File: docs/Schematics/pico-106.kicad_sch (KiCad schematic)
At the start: 22 parts, among them J1 MIDI in, J2 Debug, J3 Stereo line out, J4 Debug, Q1 2N2222A, SW1 RST, U1 Pico 2 (RP2350), U2 TL072, U3 H11L1

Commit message: Rename project pico-106
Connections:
- net MIDI 31250 baud 8-N-1: now also U1.27 (GPIO21); no longer U1.26 (GPIO20)
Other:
- company: https://github.com/AnotherJohnH/pico106 -> https://github.com/AnotherJohnH/pico-106
- title: pico106 -> pico-106
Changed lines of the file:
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@@
   (paper "A4")
   (title_block
-    (title "pico106")
-    (date "2024-10-26")
+    (title "pico-106")
+    (date "2024-10-27")
     (rev "0.01")
-    (company "https://github.com/AnotherJohnH/pico106")
+    (company "https://github.com/AnotherJohnH/pico-106")
   )
   (junction (at 220.98 62.23) (diameter 0) (color 0 0 0 0)
@@
     (stroke (width 0) (type default))
   )
-  (wire (pts (xy 46.99 63.5) (xy 40.64 63.5))
+  (wire (pts (xy 46.99 60.96) (xy 40.64 60.96))
     (stroke (width 0) (type default))
   )
@@
     (stroke (width 0) (type default))
   )
-  (wire (pts (xy 40.64 63.5) (xy 40.64 91.44))
-    (stroke (width 0) (type default))
-  )
+  (wire (pts (xy 40.64 60.96) (xy 40.64 91.44))
+    (stroke (width 0) (type default))
+  )

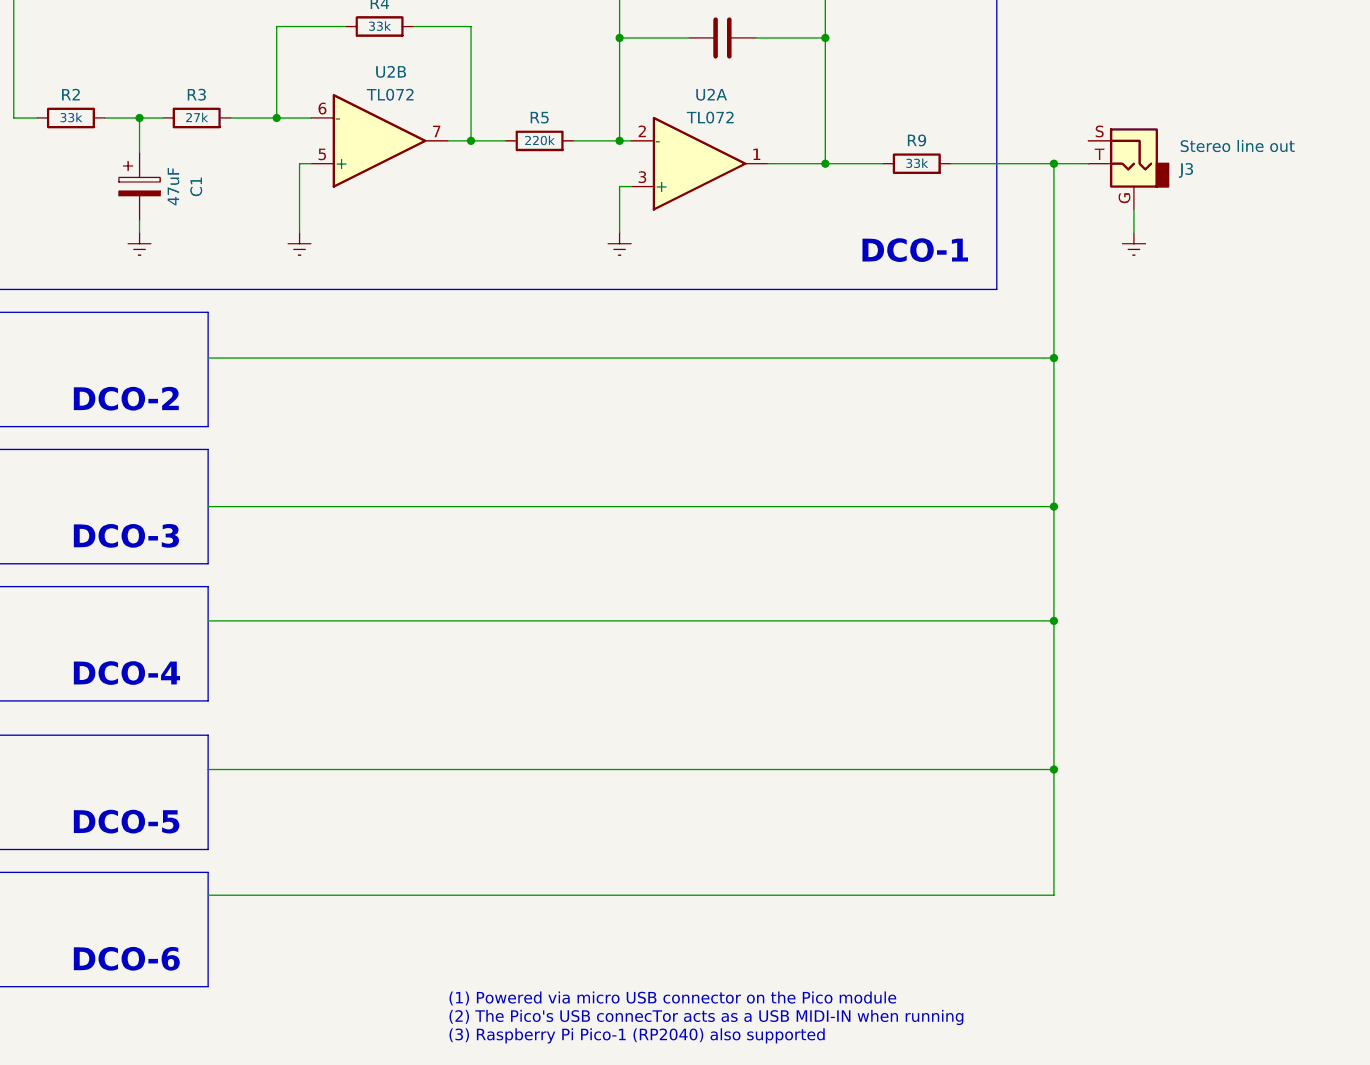
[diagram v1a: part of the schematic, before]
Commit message: Add initial spice model
  + also fixed wrong value for C1 on  schematic
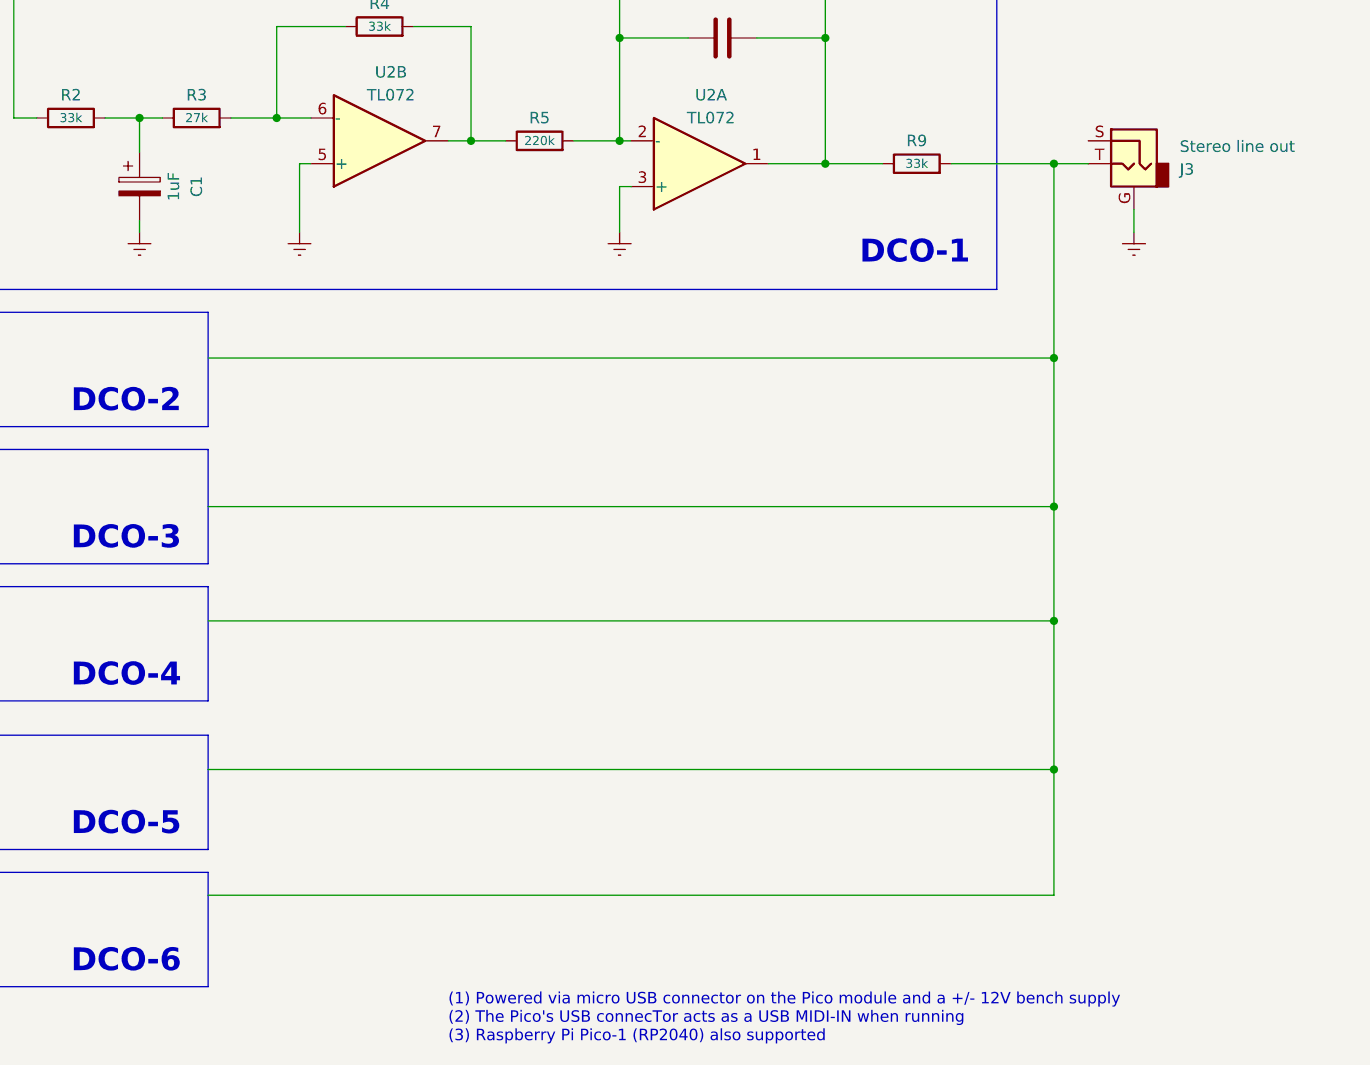
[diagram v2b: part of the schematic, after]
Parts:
- C1: value 47uF -> 1uF
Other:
- note added: "(1) Powered via micro USB connector on the Pico module and a +/- 12V bench supply (2) The Pico's USB connecTor acts as a USB MIDI-IN when running (3) Raspberry Pi Pico-1 (RP2040) also supported"
- note removed: "(1) Powered via micro USB connector on the Pico module (2) The Pico's USB connecTor acts as a USB MIDI-IN when running (3) Raspberry Pi Pico-1 (RP2040) also supported"
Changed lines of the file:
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@@
     (effects (font (size 2.54 2.54) (thickness 0.508) bold (color 84 84 84 1)) (justify left bottom))
   )
-  (text "(1) Powered via micro USB connector on the Pico module\n(2) The Pico's USB connecTor acts as a USB MIDI-IN when running\n(3) Raspberry Pi Pico-1 (RP2040) also supported"
+  (text "(1) Powered via micro USB connector on the Pico module and a +/- 12V bench supply\n(2) The Pico's USB connecTor acts as a USB MIDI-IN when running\n(3) Raspberry Pi Pico-1 (RP2040) also supported"
     (at 179.07 173.99 0)
     (effects (font (size 1.27 1.27)) (justify left bottom))
@@
     (pin "2")
     (instances
-      (project "pico106"
+      (project "pico-106"
         (path "/8dd66cb3-bd85-43a0-9ef0-1bd8a27e677c"
           (reference "R7") (unit 1)
@@
     (pin "2")
     (instances
-      (project "pico106"
+      (project "pico-106"
         (path "/8dd66cb3-bd85-43a0-9ef0-1bd8a27e677c"
           (reference "C3") (unit 1)
@@
     (pin "2")
     (instances
-      (project "pico106"
+      (project "pico-106"
         (path "/8dd66cb3-bd85-43a0-9ef0-1bd8a27e677c"
           (reference "D1") (unit 1)
@@
     (pin "9")
     (instances
-      (project "pico106"
+      (project "pico-106"
         (path "/8dd66cb3-bd85-43a0-9ef0-1bd8a27e677c"
           (reference "U1") (unit 1)
@@
     (pin "8")
     (instances
-      (project "pico106"
+      (project "pico-106"
         (path "/8dd66cb3-bd85-43a0-9ef0-1bd8a27e677c"
           (reference "U2") (unit 1)
@@
     (pin "1")
     (instances
-      (project "pico106"
+      (project "pico-106"
         (path "/8dd66cb3-bd85-43a0-9ef0-1bd8a27e677c"
           (reference "#PWR02") (unit 1)
@@
     (pin "2")
     (instances
-      (project "pico106"
+      (project "pico-106"
         (path "/8dd66cb3-bd85-43a0-9ef0-1bd8a27e677c"
           (reference "R5") (unit 1)
@@
     (pin "2")
     (instances
-      (project "pico106"
+      (project "pico-106"
         (path "/8dd66cb3-bd85-43a0-9ef0-1bd8a27e677c"
           (reference "R8") (unit 1)
@@
     (pin "3")
     (instances
-      (project "pico106"
+      (project "pico-106"
         (path "/8dd66cb3-bd85-43a0-9ef0-1bd8a27e677c"
           (reference "J2") (unit 1)
@@
     (pin "3")
     (instances
-      (project "pico106"
+      (project "pico-106"
         (path "/8dd66cb3-bd85-43a0-9ef0-1bd8a27e677c"
           (reference "Q1") (unit 1)
@@
     (pin "6")
     (instances
-      (project "pico106"
+      (project "pico-106"
         (path "/8dd66cb3-bd85-43a0-9ef0-1bd8a27e677c"
           (reference "U3") (unit 1)
@@
     (pin "1")
     (instances
-      (project "pico106"
+      (project "pico-106"
         (path "/8dd66cb3-bd85-43a0-9ef0-1bd8a27e677c"
           (reference "#PWR05") (unit 1)
@@
     (pin "2")
     (instances
-      (project "pico106"
+      (project "pico-106"
         (path "/8dd66cb3-bd85-43a0-9ef0-1bd8a27e677c"
           (reference "R2") (unit 1)
@@
     (pin "2")
     (instances
-      (project "pico106"
+      (project "pico-106"
         (path "/8dd66cb3-bd85-43a0-9ef0-1bd8a27e677c"
           (reference "SW1") (unit 1)
@@
     (pin "T")
     (instances
-      (project "pico106"
+      (project "pico-106"
         (path "/8dd66cb3-bd85-43a0-9ef0-1bd8a27e677c"
           (reference "J3") (unit 1)
@@
     (pin "1")
     (instances
-      (project "pico106"
+      (project "pico-106"
         (path "/8dd66cb3-bd85-43a0-9ef0-1bd8a27e677c"
           (reference "#PWR09") (unit 1)
@@
     (pin "1")
     (instances
-      (project "pico106"
+      (project "pico-106"
         (path "/8dd66cb3-bd85-43a0-9ef0-1bd8a27e677c"
           (reference "#PWR06") (unit 1)
@@
     (pin "2")
     (instances
-      (project "pico106"
+      (project "pico-106"
         (path "/8dd66cb3-bd85-43a0-9ef0-1bd8a27e677c"
           (reference "R3") (unit 1)
@@
     (pin "8")
     (instances
-      (project "pico106"
+      (project "pico-106"
         (path "/8dd66cb3-bd85-43a0-9ef0-1bd8a27e677c"
           (reference "U2") (unit 2)
@@
     (pin "1")
     (instances
-      (project "pico106"
+      (project "pico-106"
         (path "/8dd66cb3-bd85-43a0-9ef0-1bd8a27e677c"
           (reference "#PWR011") (unit 1)
@@
     (pin "2")
     (instances
-      (project "pico106"
+      (project "pico-106"
         (path "/8dd66cb3-bd85-43a0-9ef0-1bd8a27e677c"
           (reference "R9") (unit 1)
@@
     (pin "5")
     (instances
-      (project "pico106"
+      (project "pico-106"
         (path "/8dd66cb3-bd85-43a0-9ef0-1bd8a27e677c"
           (reference "J1") (unit 1)
@@
     (pin "2")
     (instances
-      (project "pico106"
+      (project "pico-106"
         (path "/8dd66cb3-bd85-43a0-9ef0-1bd8a27e677c"
           (reference "R1") (unit 1)
@@
     (pin "2")
     (instances
-      (project "pico106"
+      (project "pico-106"
         (path "/8dd66cb3-bd85-43a0-9ef0-1bd8a27e677c"
           (reference "C2") (unit 1)
@@
     (pin "2")
     (instances
-      (project "pico106"
+      (project "pico-106"
         (path "/8dd66cb3-bd85-43a0-9ef0-1bd8a27e677c"
           (reference "R4") (unit 1)
@@
       (effects (font (size 1.27 1.27)))
     )
-    (property "Value" "47uF" (at 148.59 78.74 90)
+    (property "Value" "1uF" (at 148.59 78.74 90)
       (effects (font (size 1.27 1.27)))
     )
@@
     (pin "2")
     (instances
-      (project "pico106"
+      (project "pico-106"
         (path "/8dd66cb3-bd85-43a0-9ef0-1bd8a27e677c"
           (reference "C1") (unit 1)
@@
     (pin "1")
     (instances
-      (project "pico106"
+      (project "pico-106"
         (path "/8dd66cb3-bd85-43a0-9ef0-1bd8a27e677c"
           (reference "#PWR08") (unit 1)
@@
     (pin "1")
     (instances
-      (project "pico106"
+      (project "pico-106"
         (path "/8dd66cb3-bd85-43a0-9ef0-1bd8a27e677c"
           (reference "#PWR01") (unit 1)
@@
     (pin "3")
     (instances
-      (project "pico106"
+      (project "pico-106"
         (path "/8dd66cb3-bd85-43a0-9ef0-1bd8a27e677c"
           (reference "J4") (unit 1)
@@
     (pin "1")
     (instances
-      (project "pico106"
+      (project "pico-106"
         (path "/8dd66cb3-bd85-43a0-9ef0-1bd8a27e677c"
           (reference "#PWR010") (unit 1)
@@
     (pin "1")
     (instances
-      (project "pico106"
+      (project "pico-106"
         (path "/8dd66cb3-bd85-43a0-9ef0-1bd8a27e677c"
           (reference "#PWR03") (unit 1)
@@
     (pin "1")
     (instances
-      (project "pico106"
+      (project "pico-106"
         (path "/8dd66cb3-bd85-43a0-9ef0-1bd8a27e677c"
           (reference "#PWR04") (unit 1)
@@
     (pin "2")
     (instances
-      (project "pico106"
+      (project "pico-106"
         (path "/8dd66cb3-bd85-43a0-9ef0-1bd8a27e677c"
           (reference "R6") (unit 1)
@@
     (pin "1")
     (instances
-      (project "pico106"
+      (project "pico-106"
         (path "/8dd66cb3-bd85-43a0-9ef0-1bd8a27e677c"
           (reference "#PWR07") (unit 1)

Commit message: Increase DAC frequency (software and hardware change) for better quality waveform
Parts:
- removed C1: 1uF, symbol Device:C_Polarized
- added C1: 22nF, symbol Device:C
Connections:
- net Earth: now also C1.1
- net at R2.2, R3.1: now also C1.2
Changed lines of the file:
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@@
+    )
+  )
+  (symbol (lib_id "Device:C") (at 144.78 78.74 0) (mirror x) (unit 1)
+    (in_bom yes) (on_board yes) (dnp no) (fields_autoplaced)
+    (property "Reference" "C1" (at 140.97 77.47 0)
+      (effects (font (size 1.27 1.27)) (justify right))
+    )
+    (property "Value" "22nF" (at 140.97 80.01 0)
+      (effects (font (size 1.27 1.27)) (justify right))
+    )
+    (property "Footprint" "" (at 145.7452 74.93 0)
+      (effects (font (size 1.27 1.27)) hide)
+    )
+    (property "Datasheet" "~" (at 144.78 78.74 0)
+      (effects (font (size 1.27 1.27)) hide)
+    )
+    (pin "1")
+    (pin "2")
+    (instances
+      (project "pico-106"
+        (path "/8dd66cb3-bd85-43a0-9ef0-1bd8a27e677c"
+          (reference "C1") (unit 1)
+        )
+      )
     )
   )
@@
         )
       )
-    )
-  )
-  (symbol (lib_id "Device:C_Polarized") (at 144.78 78.74 0) (unit 1)
-    (in_bom yes) (on_board yes) (dnp no)
-    (property "Reference" "C1" (at 151.13 78.74 90)
-      (effects (font (size 1.27 1.27)))
-    )
-    (property "Value" "1uF" (at 148.59 78.74 90)
-      (effects (font (size 1.27 1.27)))
-    )
-    (property "Footprint" "" (at 145.7452 82.55 0)
-      (effects (font (size 1.27 1.27)) hide)
-    )
-    (property "Datasheet" "~" (at 144.78 78.74 0)
-      (effects (font (size 1.27 1.27)) hide)
-    )
-    (pin "1")
-    (pin "2")
-    (instances
-      (project "pico-106"
-        (path "/8dd66cb3-bd85-43a0-9ef0-1bd8a27e677c"
-          (reference "C1") (unit 1)
-        )
-      )

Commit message: Capture latest docs
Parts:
- added C4: 22nF, Capacitor_THT:C_Disc_D5.0mm_W2.5mm_P5.00mm, symbol Device:C
- added unit 3 of U2
- C1, C2, C3: footprint (none) -> Capacitor_THT:C_Disc_D5.0mm_W2.5mm_P5.00mm
- Q1: footprint Package_TO_SOT_THT:TO-39-3 -> Package_TO_SOT_THT:TO-92
- R7: footprint esistor_THT:R_Axial_DIN0204_L3.6mm_D1.6mm_P5.08mm_Horizontal -> Resistor_THT:R_Axial_DIN0204_L3.6mm_D1.6mm_P5.08mm_Horizontal
- U1: footprint RPi_Pico:RPi_Pico_SMD_TH -> Package_DIP:DIP-40_W25.4mm_Socket
- U2: footprint (none) -> Package_DIP:DIP-8_W7.62mm_Socket
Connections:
- net at C3.2, R8.2, U2.1: now also C4.1; no longer R9.1
- new net: C4.2, R9.1
- new net +12V: U2.8 (V+)
- new net -12V: U2.4 (V-)
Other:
- note added: "(1) Powered via micro USB connector on the Pico module and a +/- 12V supply (2) The Pico's USB connecTor acts as a USB MIDI-IN when running (3) Raspberry Pi Pico-1 (RP2040) also supported"
- note removed: "(1) Powered via micro USB connector on the Pico module and a +/- 12V bench supply (2) The Pico's USB connecTor acts as a USB MIDI-IN when running (3) Raspberry Pi Pico-1 (RP2040) also supported"
- moved on the sheet: J3, R9
